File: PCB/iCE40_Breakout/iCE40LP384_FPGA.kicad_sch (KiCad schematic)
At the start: 31 parts, among them J3 Conn_01x10, J5 Conn_01x10, J6 Conn_01x08, Q1 L2N7002SLLT1G, SW1 KH-6X6X5H-STM, U1 ICE40LP384-SG32

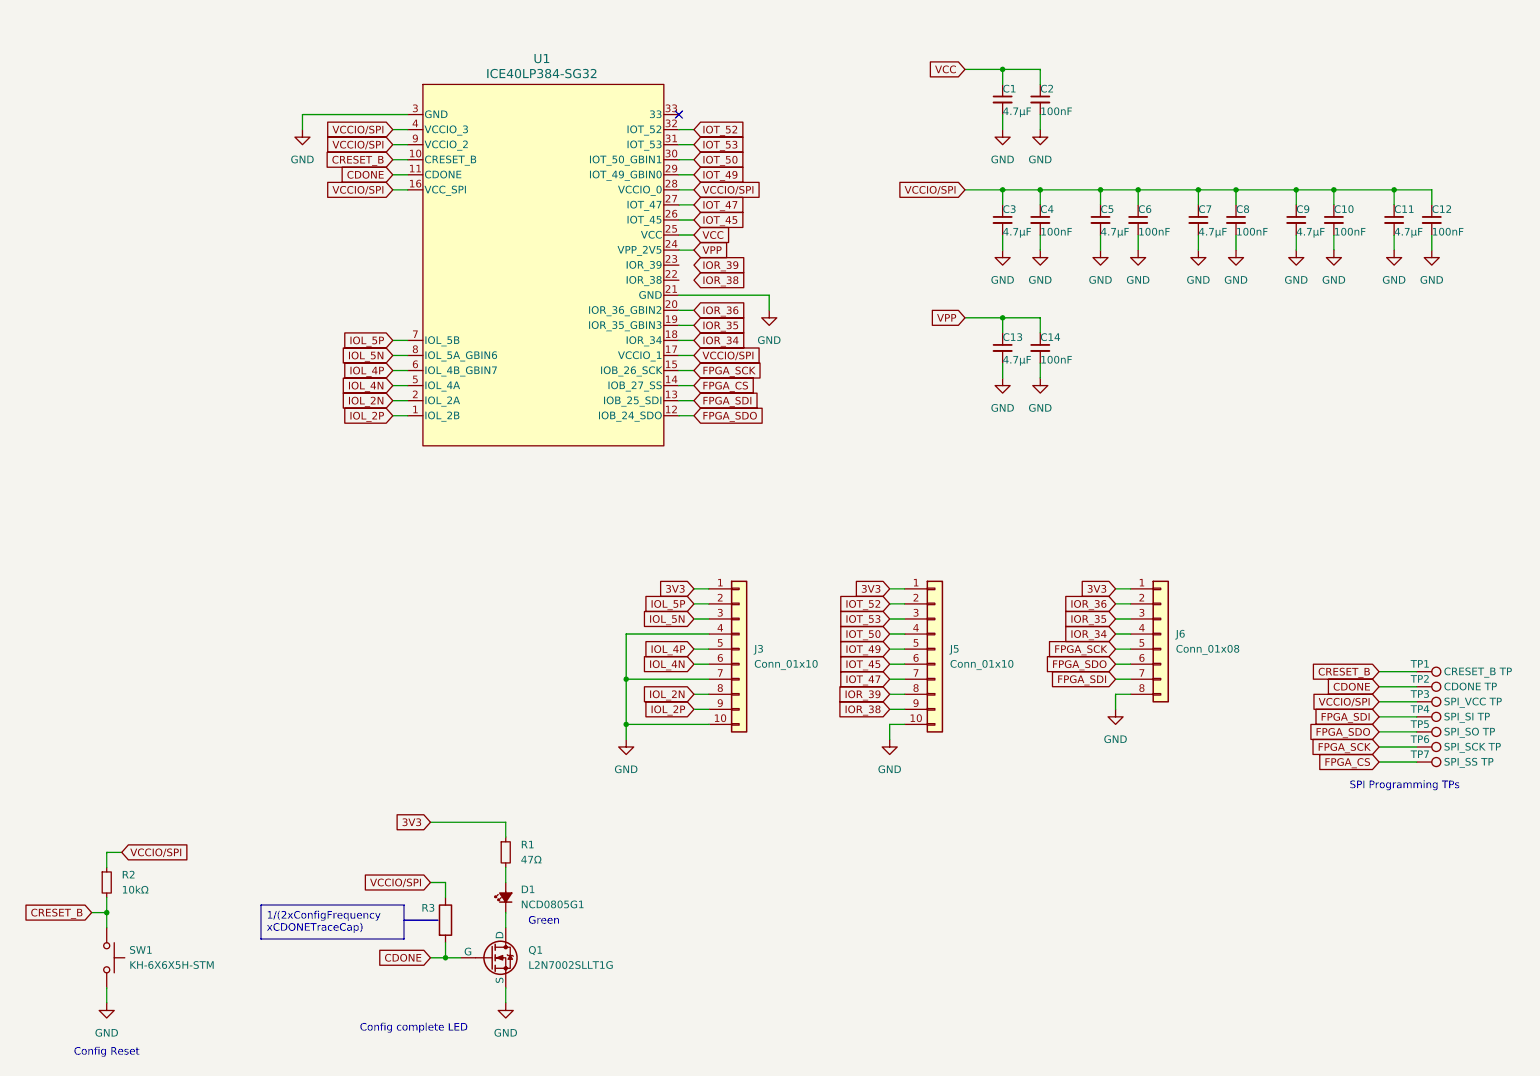
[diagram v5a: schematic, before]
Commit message: Added sheet information, and fixed ERC errors
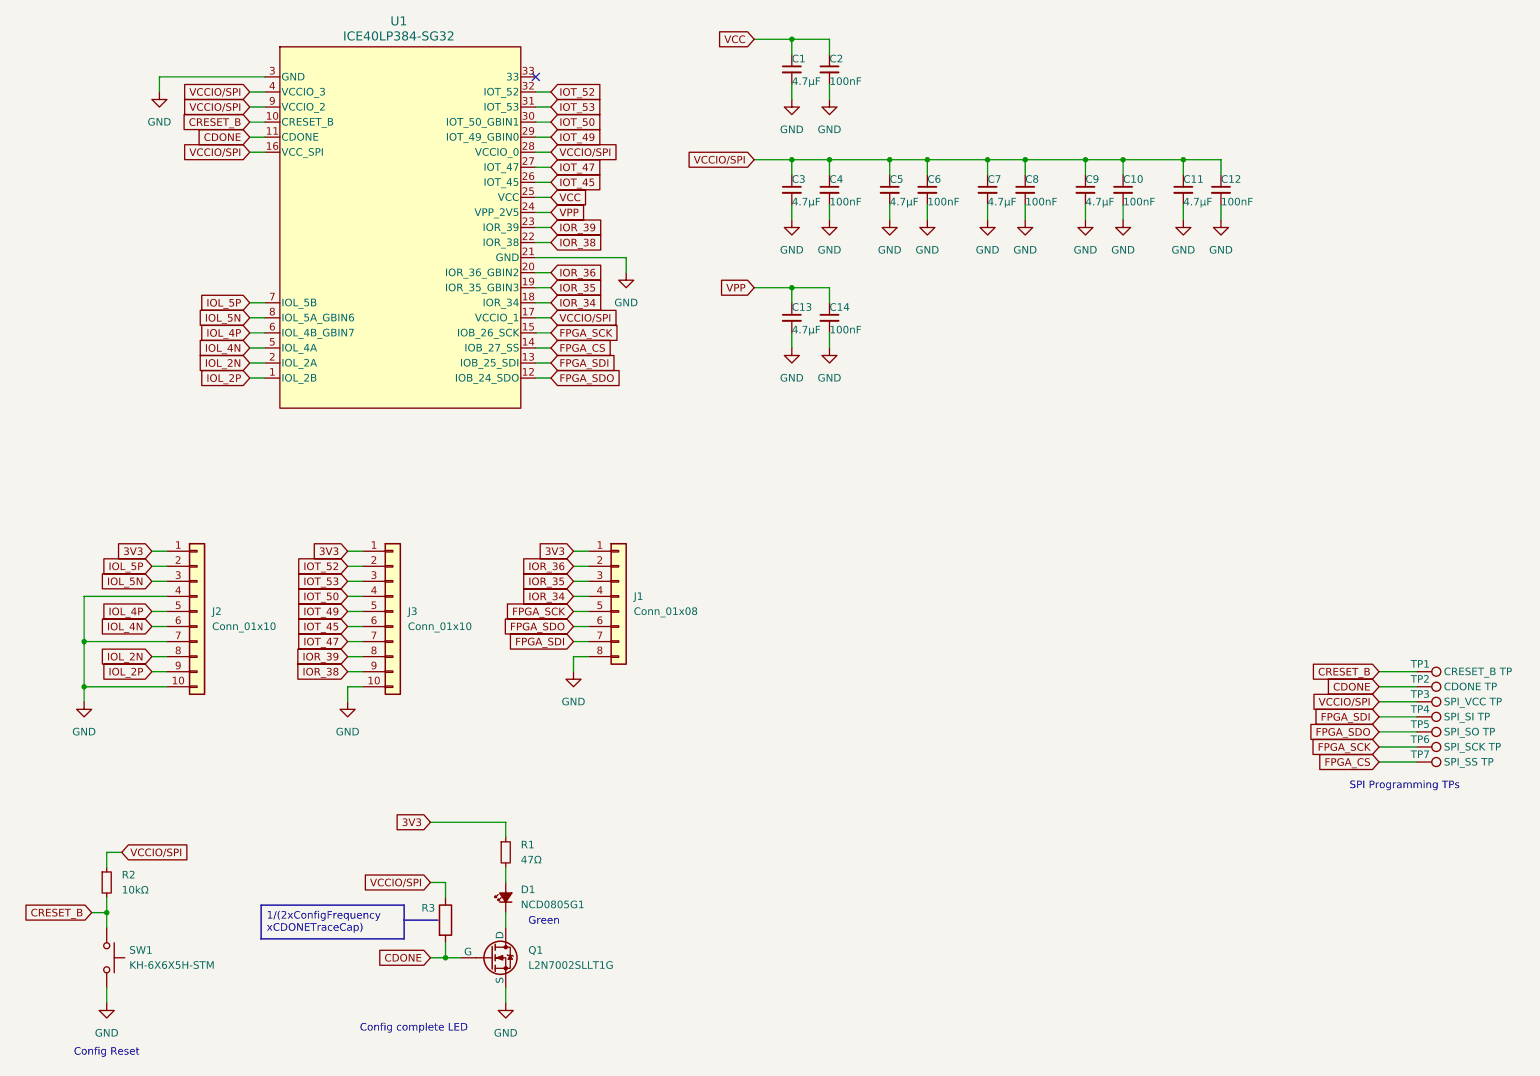
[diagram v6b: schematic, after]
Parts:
- renumbered J6 to J1, J3 to J2, J5 to J3
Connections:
- net IOR_38: now also U1.22 (IOR_38)
- net IOR_39: now also U1.23 (IOR_39)
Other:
- company: (none) -> S3I
- title: (none) -> iCE40 Breakout
- moved on the sheet: C1, C10, C11, C12, C13, C14, C2, C3, C4, C5, C6, C7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

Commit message: Added missing footprints
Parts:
- J1: footprint (none) -> Connector_PinHeader_2.54mm:PinHeader_1x08_P2.54mm_Vertical
- J2, J3: footprint (none) -> Connector_PinHeader_2.54mm:PinHeader_1x10_P2.54mm_Vertical
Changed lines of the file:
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@@
 			)
 		)
-		(property "Footprint" ""
+		(property "Footprint" "Connector_PinHeader_2.54mm:PinHeader_1x10_P2.54mm_Vertical"
 			(at 49.53 120.65 0)
 			(effects
@@
 			)
 		)
-		(property "Footprint" ""
+		(property "Footprint" "Connector_PinHeader_2.54mm:PinHeader_1x08_P2.54mm_Vertical"
 			(at 120.65 118.11 0)
 			(effects
@@
 			)
 		)
-		(property "Footprint" ""
+		(property "Footprint" "Connector_PinHeader_2.54mm:PinHeader_1x10_P2.54mm_Vertical"
 			(at 82.55 120.65 0)
 			(effects

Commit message: Changed LED footprints to be from LED lib, and not the Diode lib
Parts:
- D1: footprint Diode_SMD:D_0805_2012Metric -> LED_SMD:LED_0805_2012Metric
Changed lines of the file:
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@@
 			)
 		)
-		(property "Footprint" "Diode_SMD:D_0805_2012Metric"
+		(property "Footprint" "LED_SMD:LED_0805_2012Metric"
 			(at 101.6 168.91 90)
 			(effects
